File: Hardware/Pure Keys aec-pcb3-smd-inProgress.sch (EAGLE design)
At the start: 72 parts, among them Q2 20MHz, U1 ATMEGA328P_TQFP

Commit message: reroutes
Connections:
- net 5V: now also U1.VCC@6
- net GND: now also 75151-2A.D5, 75151-2A.D6, 75151-2A.D7, U1.AGND
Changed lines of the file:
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@@
 <part name="R2" library="rcl" deviceset="R-US_" device="R0805" value="330R"/>
 <part name="CLOCK" library="INSTRUO" deviceset="TRANSISTOR_MMBT3904" device="" value="2N3904"/>
-<part name="GND11" library="supply1" library_urn="urn:adsk.eagle:library:371" deviceset="GND" device=""/>
 <part name="R5" library="rcl" deviceset="R-US_" device="R0805" value="10K"/>
-<part name="SUPPLY9" library="supply2" deviceset="+5V" device=""/>
 <part name="R6" library="rcl" deviceset="R-US_" device="R0805" value="100K"/>
 <part name="R7" library="rcl" deviceset="R-US_" device="R0805" value="1M"/>
-<part name="GND12" library="supply1" library_urn="urn:adsk.eagle:library:371" deviceset="GND" device=""/>
 <part name="CLK_IN" library="GMSN" deviceset="PJ302M" device="" value="PJ302M"/>
-<part name="GND13" library="supply1" library_urn="urn:adsk.eagle:library:371" deviceset="GND" device=""/>
 <part name="REF" library="GMSN-R2Project" deviceset="LM4040A30IDBZT" device="" value="LM4040">
 <attribute name="MPN" value="LM4040A30IDBZT"/>
@@
 </segment>
 <segment>
-<wire x1="17.78" y1="111.76" x2="15.24" y2="111.76" width="0.1524" layer="91"/>
-<wire x1="15.24" y1="111.76" x2="15.24" y2="109.22" width="0.1524" layer="91"/>
-<wire x1="15.24" y1="109.22" x2="17.78" y2="109.22" width="0.1524" layer="91"/>
-<wire x1="15.24" y1="109.22" x2="12.7" y2="109.22" width="0.1524" layer="91"/>
-<junction x="15.24" y="109.22"/>
-<label x="12.7" y="109.22" size="1.778" layer="95" rot="R180"/>
-<pinref part="U1" gate="U$1" pin="GND@3"/>
-<pinref part="U1" gate="U$1" pin="GND@5"/>
-</segment>
-<segment>
 <pinref part="C17" gate="G$1" pin="2"/>
 <wire x1="-5.08" y1="142.24" x2="-10.16" y2="142.24" width="0.1524" layer="91"/>
@@
 <label x="165.1" y="83.82" size="1.778" layer="95"/>
 </segment>
+<segment>
+<pinref part="75151-2" gate="A" pin="D5"/>
+<wire x1="208.28" y1="96.52" x2="205.74" y2="96.52" width="0.1524" layer="91"/>
+<label x="198.12" y="96.52" size="1.778" layer="95"/>
+</segment>
+<segment>
+<pinref part="75151-2" gate="A" pin="D6"/>
+<wire x1="208.28" y1="93.98" x2="205.74" y2="93.98" width="0.1524" layer="91"/>
+<label x="198.12" y="93.98" size="1.778" layer="95"/>
+</segment>
+<segment>
+<pinref part="75151-2" gate="A" pin="D7"/>
+<wire x1="208.28" y1="91.44" x2="205.74" y2="91.44" width="0.1524" layer="91"/>
+<label x="198.12" y="91.44" size="1.778" layer="95"/>
+</segment>
+<segment>
+<pinref part="U1" gate="U$1" pin="GND@5"/>
+<wire x1="17.78" y1="109.22" x2="15.24" y2="109.22" width="0.1524" layer="91"/>
+<pinref part="U1" gate="U$1" pin="GND@3"/>
+<wire x1="15.24" y1="109.22" x2="10.16" y2="109.22" width="0.1524" layer="91"/>
+<wire x1="17.78" y1="111.76" x2="15.24" y2="111.76" width="0.1524" layer="91"/>
+<wire x1="15.24" y1="111.76" x2="15.24" y2="109.22" width="0.1524" layer="91"/>
+<junction x="15.24" y="109.22"/>
+<pinref part="U1" gate="U$1" pin="AGND"/>
+<wire x1="17.78" y1="114.3" x2="15.24" y2="114.3" width="0.1524" layer="91"/>
+<wire x1="15.24" y1="114.3" x2="15.24" y2="111.76" width="0.1524" layer="91"/>
+<junction x="15.24" y="111.76"/>
+<label x="10.16" y="109.22" size="1.778" layer="95"/>
+</segment>
 </net>
 <net name="RST" class="0">
@@
 <segment>
 <label x="15.24" y="165.1" size="1.778" layer="95" rot="R180"/>
-<wire x1="20.32" y1="165.1" x2="17.78" y2="165.1" width="0.1524" layer="91"/>
 <pinref part="U1" gate="U$1" pin="PC6(/RESET)"/>
 <wire x1="17.78" y1="165.1" x2="15.24" y2="165.1" width="0.1524" layer="91"/>
-<junction x="17.78" y="165.1"/>
 </segment>
 </net>
@@
 </segment>
 <segment>
-<wire x1="17.78" y1="160.02" x2="15.24" y2="160.02" width="0.1524" layer="91"/>
-<wire x1="17.78" y1="157.48" x2="15.24" y2="157.48" width="0.1524" layer="91"/>
-<wire x1="15.24" y1="157.48" x2="15.24" y2="160.02" width="0.1524" layer="91"/>
-<junction x="15.24" y="160.02"/>
-<label x="12.7" y="160.02" size="1.778" layer="95" rot="R180"/>
-<wire x1="15.24" y1="160.02" x2="12.7" y2="160.02" width="0.1524" layer="91"/>
-<pinref part="U1" gate="U$1" pin="VCC@4"/>
-<pinref part="U1" gate="U$1" pin="AVCC"/>
-</segment>
-<segment>
 <pinref part="74151-1" gate="P" pin="VCC"/>
 <wire x1="256.54" y1="162.56" x2="256.54" y2="165.1" width="0.1524" layer="91"/>
@@
 <wire x1="165.1" y1="101.6" x2="165.1" y2="104.14" width="0.1524" layer="91"/>
 <label x="165.1" y="104.14" size="1.778" layer="95"/>
+</segment>
+<segment>
+<pinref part="U1" gate="U$1" pin="AVCC"/>
+<wire x1="17.78" y1="160.02" x2="15.24" y2="160.02" width="0.1524" layer="91"/>
+<pinref part="U1" gate="U$1" pin="VCC@6"/>
+<wire x1="15.24" y1="160.02" x2="12.7" y2="160.02" width="0.1524" layer="91"/>
+<wire x1="17.78" y1="154.94" x2="15.24" y2="154.94" width="0.1524" layer="91"/>
+<wire x1="15.24" y1="154.94" x2="15.24" y2="157.48" width="0.1524" layer="91"/>
+<junction x="15.24" y="160.02"/>
+<pinref part="U1" gate="U$1" pin="VCC@4"/>
+<wire x1="15.24" y1="157.48" x2="15.24" y2="160.02" width="0.1524" layer="91"/>
+<wire x1="17.78" y1="157.48" x2="15.24" y2="157.48" width="0.1524" layer="91"/>
+<junction x="15.24" y="157.48"/>
+<label x="7.62" y="160.02" size="1.778" layer="95"/>
 </segment>
 </net>
@@
 <wire x1="99.06" y1="73.66" x2="81.28" y2="73.66" width="0.1524" layer="91"/>
 <junction x="99.06" y="73.66"/>
+<label x="73.66" y="73.66" size="1.778" layer="95"/>
 </segment>
 <segment>
@@
 <wire x1="99.06" y1="116.84" x2="81.28" y2="116.84" width="0.1524" layer="91"/>
 <junction x="99.06" y="116.84"/>
+<label x="76.2" y="116.84" size="1.778" layer="95"/>
 </segment>
 </net>
@@
 <instances>
 <instance part="CLOCK" gate="G$1" x="106.68" y="91.44" rot="R90"/>
-<instance part="GND11" gate="1" x="111.76" y="73.66" rot="MR0"/>
 <instance part="R5" gate="G$1" x="111.76" y="114.3" rot="MR90"/>
-<instance part="SUPPLY9" gate="+5V" x="111.76" y="124.46" rot="MR0"/>
 <instance part="R6" gate="G$1" x="78.74" y="91.44" rot="MR0"/>
 <instance part="R7" gate="G$1" x="88.9" y="83.82" rot="MR90"/>
-<instance part="GND12" gate="1" x="88.9" y="73.66" rot="MR0"/>
 <instance part="CLK_IN" gate="G$1" x="60.96" y="88.9" rot="MR0"/>
-<instance part="GND13" gate="1" x="68.58" y="81.28" rot="MR0"/>
 </instances>
 <busses>
 </busses>
 <nets>
-<net name="GND" class="1">
-<segment>
-<pinref part="CLOCK" gate="G$1" pin="E"/>
-<wire x1="111.76" y1="78.74" x2="111.76" y2="76.2" width="0.1524" layer="91"/>
-<pinref part="GND11" gate="1" pin="GND"/>
-</segment>
-<segment>
-<pinref part="R7" gate="G$1" pin="1"/>
-<wire x1="88.9" y1="78.74" x2="88.9" y2="76.2" width="0.1524" layer="91"/>
-<pinref part="GND12" gate="1" pin="GND"/>
-</segment>
-<segment>
-<pinref part="CLK_IN" gate="G$1" pin="SLEEVE"/>
-<wire x1="66.04" y1="86.36" x2="68.58" y2="86.36" width="0.1524" layer="91"/>
-<wire x1="68.58" y1="86.36" x2="68.58" y2="83.82" width="0.1524" layer="91"/>
-<pinref part="GND13" gate="1" pin="GND"/>
-</segment>
-</net>
 <net name="5V" class="1">
 <segment>
 <pinref part="R5" gate="G$1" pin="2"/>
-<pinref part="SUPPLY9" gate="+5V" pin="+5V"/>
 <wire x1="111.76" y1="121.92" x2="111.76" y2="119.38" width="0.1524" layer="91"/>
+<label x="111.76" y="121.92" size="1.778" layer="95"/>
 </segment>
 </net>
@@
 </segment>
 </net>
+<net name="GND" class="1">
+<segment>
+<pinref part="CLOCK" gate="G$1" pin="E"/>
+<wire x1="111.76" y1="78.74" x2="111.76" y2="76.2" width="0.1524" layer="91"/>
+<label x="111.76" y="76.2" size="1.778" layer="95"/>
+</segment>
+<segment>
+<pinref part="R7" gate="G$1" pin="1"/>
+<wire x1="88.9" y1="78.74" x2="88.9" y2="76.2" width="0.1524" layer="91"/>
+<label x="88.9" y="76.2" size="1.778" layer="95"/>
+</segment>
+<segment>
+<pinref part="CLK_IN" gate="G$1" pin="SLEEVE"/>
+<wire x1="66.04" y1="86.36" x2="68.58" y2="86.36" width="0.1524" layer="91"/>
+<wire x1="68.58" y1="86.36" x2="68.58" y2="83.82" width="0.1524" layer="91"/>
+<label x="68.58" y="83.82" size="1.778" layer="95"/>
+</segment>
+</net>

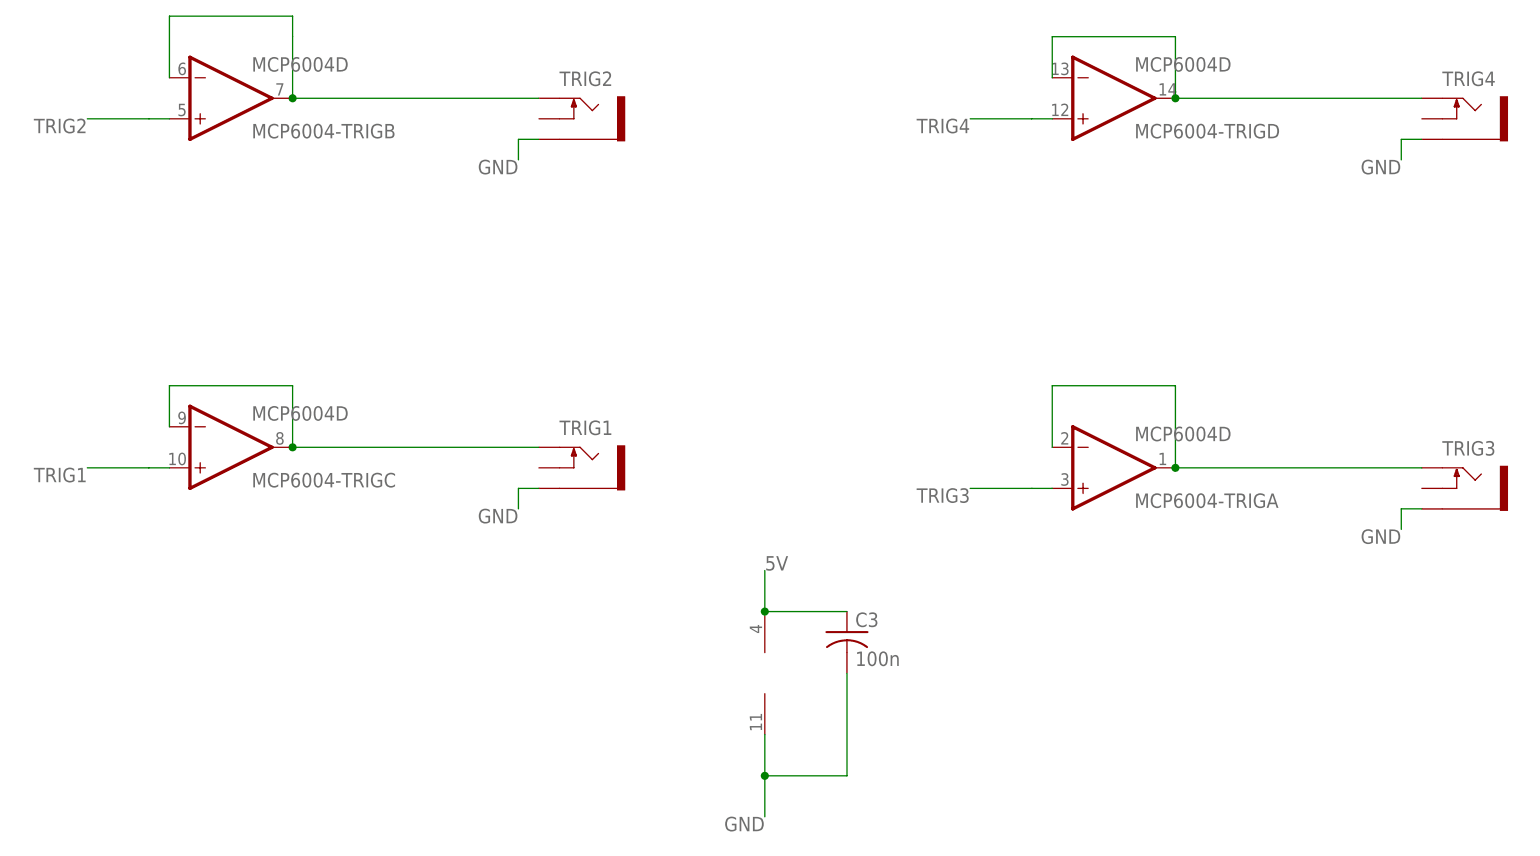
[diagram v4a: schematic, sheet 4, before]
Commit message: Replaced Sockets with vertical type
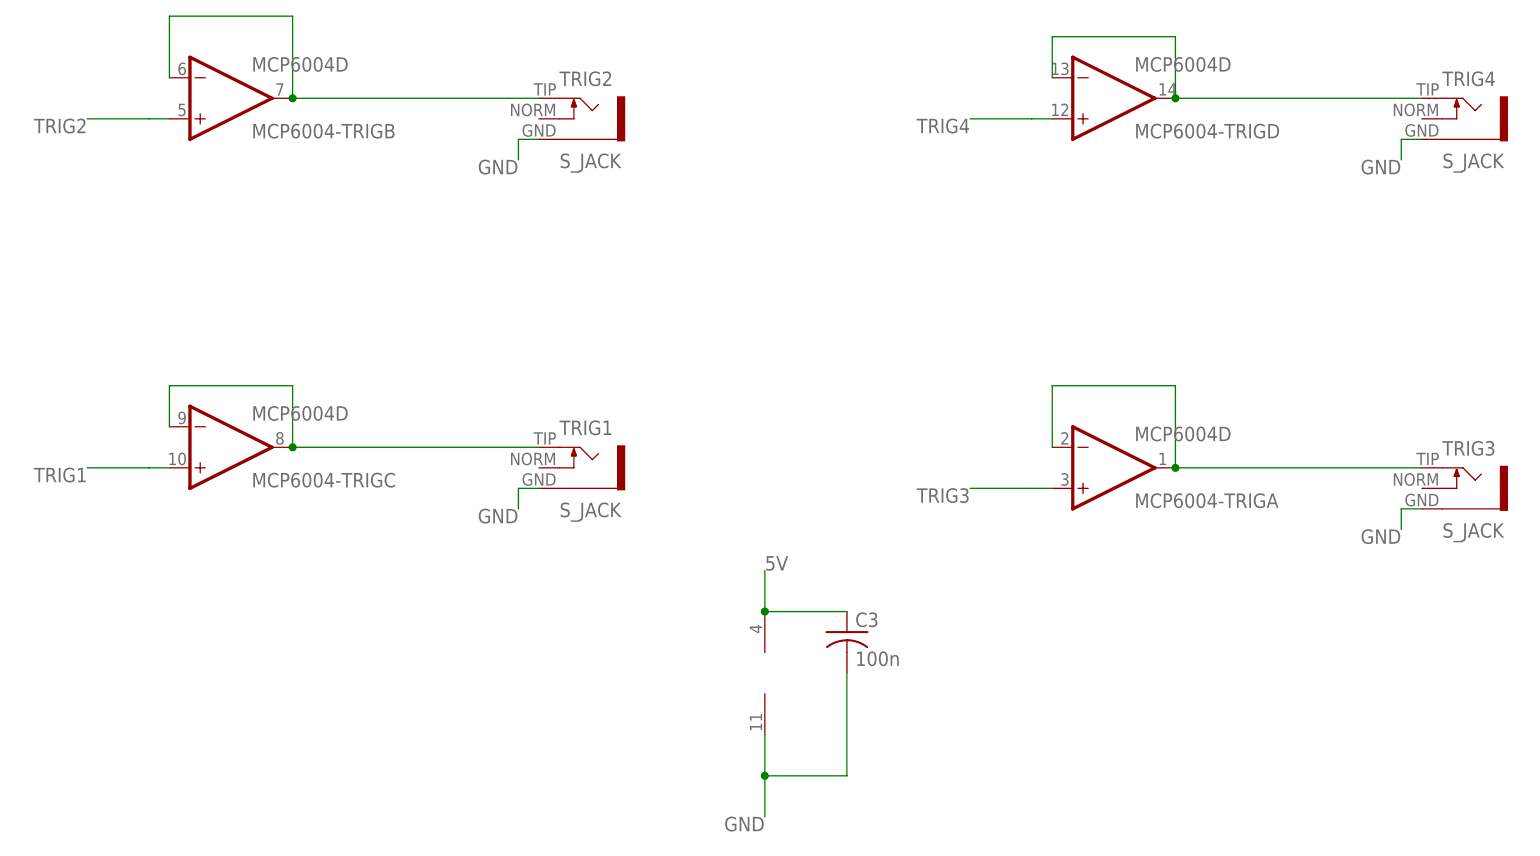
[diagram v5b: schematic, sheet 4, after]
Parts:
- CLK_IN, CV1, CV2, CV3, CV4, TRIG1, TRIG2, TRIG3, TRIG4: value PJ302M -> S_JACK; device GMSN:PJ302M -> INSTRUO:S_JACK
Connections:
- net GND: now also CLK_IN.GND, CV1.GND, CV2.GND, CV3.GND, CV4.GND, TRIG1.GND, TRIG2.GND, TRIG3.GND, TRIG4.GND; no longer CLK_IN.SLEEVE, CV1.SLEEVE, CV2.SLEEVE, CV3.SLEEVE, CV4.SLEEVE, TRIG1.SLEEVE, TRIG2.SLEEVE, TRIG3.SLEEVE, TRIG4.SLEEVE
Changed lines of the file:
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@@
 <class number="0" name="default" width="0" drill="0">
 </class>
-<class number="1" name="Power" width="0.8" drill="0">
+<class number="1" name="Power" width="0.6096" drill="0">
 </class>
 </classes>
@@
 <part name="ISP1" library="adafruit" deviceset="AVRISP" device="-6"/>
 <part name="C4" library="rcl" deviceset="CPOL-US" device="153CLV-0505" value="10u"/>
-<part name="CV1" library="GMSN" deviceset="PJ302M" device="" value="PJ302M"/>
-<part name="TRIG1" library="GMSN" deviceset="PJ302M" device="" value="PJ302M"/>
+<part name="CV1" library="INSTRUO" deviceset="S_JACK" device="" value="S_JACK"/>
+<part name="TRIG1" library="INSTRUO" deviceset="S_JACK" device="" value="S_JACK"/>
 <part name="R15" library="rcl" deviceset="R-US_" device="R0805" value="10K"/>
 <part name="R16" library="rcl" deviceset="R-US_" device="R0805" value="10K"/>
@@
 <attribute name="RS-PART" value="669-5364"/>
 </part>
-<part name="TRIG2" library="GMSN" deviceset="PJ302M" device="" value="PJ302M"/>
-<part name="TRIG3" library="GMSN" deviceset="PJ302M" device="" value="PJ302M"/>
-<part name="TRIG4" library="GMSN" deviceset="PJ302M" device="" value="PJ302M"/>
+<part name="TRIG2" library="INSTRUO" deviceset="S_JACK" device="" value="S_JACK"/>
+<part name="TRIG3" library="INSTRUO" deviceset="S_JACK" device="" value="S_JACK"/>
+<part name="TRIG4" library="INSTRUO" deviceset="S_JACK" device="" value="S_JACK"/>
 <part name="MCP6004-V" library="GMSN-R2Project" deviceset="MCP6004" device="D" value="MCP6004D"/>
-<part name="CV2" library="GMSN" deviceset="PJ302M" device="" value="PJ302M"/>
-<part name="CV3" library="GMSN" deviceset="PJ302M" device="" value="PJ302M"/>
-<part name="CV4" library="GMSN" deviceset="PJ302M" device="" value="PJ302M"/>
+<part name="CV2" library="INSTRUO" deviceset="S_JACK" device="" value="S_JACK"/>
+<part name="CV3" library="INSTRUO" deviceset="S_JACK" device="" value="S_JACK"/>
+<part name="CV4" library="INSTRUO" deviceset="S_JACK" device="" value="S_JACK"/>
 <part name="C6" library="rcl" deviceset="C-US" device="C0805K" value="10u"/>
 <part name="C11" library="rcl" deviceset="C-US" device="C0805K" value="100n"/>
@@
 <part name="R6" library="rcl" deviceset="R-US_" device="R0805" value="100K"/>
 <part name="R7" library="rcl" deviceset="R-US_" device="R0805" value="1M"/>
-<part name="CLK_IN" library="GMSN" deviceset="PJ302M" device="" value="PJ302M"/>
+<part name="CLK_IN" library="INSTRUO" deviceset="S_JACK" device="" value="S_JACK"/>
 <part name="REF" library="GMSN-R2Project" deviceset="LM4040A30IDBZT" device="" value="LM4040">
 <attribute name="MPN" value="LM4040A30IDBZT"/>
@@
 </busses>
 <nets>
-<net name="GND" class="0">
+<net name="GND" class="1">
 <segment>
 <pinref part="ISP1" gate="G$1" pin="GND"/>
@@
 </segment>
 </net>
-<net name="5V" class="0">
+<net name="5V" class="1">
 <segment>
 <pinref part="ISP1" gate="G$1" pin="VCC"/>
@@
 </busses>
 <nets>
-<net name="5V" class="0">
+<net name="5V" class="1">
 <segment>
 <pinref part="JP2" gate="G$1" pin="VBUS"/>
@@
 </segment>
 </net>
-<net name="GND" class="0">
+<net name="GND" class="1">
 <segment>
 <pinref part="JP2" gate="G$1" pin="GND"/>
@@
 </segment>
 </net>
-<net name="GND" class="0">
+<net name="GND" class="1">
 <segment>
 <pinref part="R18" gate="G$1" pin="1"/>
@@
 </busses>
 <nets>
-<net name="GND" class="0">
+<net name="GND" class="1">
 <segment>
 <pinref part="MCP6004-TRIG" gate="P" pin="V-"/>
@@
 </segment>
 <segment>
-<pinref part="TRIG2" gate="G$1" pin="SLEEVE"/>
+<pinref part="TRIG2" gate="G$1" pin="GND"/>
 <wire x1="91.44" y1="96.52" x2="88.9" y2="96.52" width="0.1524" layer="91"/>
 <wire x1="88.9" y1="96.52" x2="88.9" y2="93.98" width="0.1524" layer="91"/>
@@
 </segment>
 <segment>
-<pinref part="TRIG1" gate="G$1" pin="SLEEVE"/>
+<pinref part="TRIG1" gate="G$1" pin="GND"/>
 <wire x1="91.44" y1="53.34" x2="88.9" y2="53.34" width="0.1524" layer="91"/>
 <wire x1="88.9" y1="53.34" x2="88.9" y2="50.8" width="0.1524" layer="91"/>
@@
 </segment>
 <segment>
-<pinref part="TRIG4" gate="G$1" pin="SLEEVE"/>
+<pinref part="TRIG4" gate="G$1" pin="GND"/>
 <wire x1="200.66" y1="96.52" x2="198.12" y2="96.52" width="0.1524" layer="91"/>
 <wire x1="198.12" y1="96.52" x2="198.12" y2="93.98" width="0.1524" layer="91"/>
@@
 </segment>
 <segment>
-<pinref part="TRIG3" gate="G$1" pin="SLEEVE"/>
+<pinref part="TRIG3" gate="G$1" pin="GND"/>
 <wire x1="200.66" y1="50.8" x2="198.12" y2="50.8" width="0.1524" layer="91"/>
 <wire x1="198.12" y1="50.8" x2="198.12" y2="48.26" width="0.1524" layer="91"/>
@@
 </segment>
 </net>
-<net name="5V" class="0">
+<net name="5V" class="1">
 <segment>
 <pinref part="C3" gate="G$1" pin="1"/>
@@
 </segment>
 </net>
-<net name="5V" class="0">
+<net name="5V" class="1">
 <segment>
 <pinref part="C6" gate="G$1" pin="1"/>
@@
 </segment>
 </net>
-<net name="GND" class="0">
-<segment>
-<pinref part="CV4" gate="G$1" pin="SLEEVE"/>
+<net name="GND" class="1">
+<segment>
+<pinref part="CV4" gate="G$1" pin="GND"/>
 <wire x1="157.48" y1="2.54" x2="154.94" y2="2.54" width="0.1524" layer="91"/>
 <wire x1="154.94" y1="2.54" x2="154.94" y2="-7.62" width="0.1524" layer="91"/>
@@
 </segment>
 <segment>
-<pinref part="CV3" gate="G$1" pin="SLEEVE"/>
+<pinref part="CV3" gate="G$1" pin="GND"/>
 <wire x1="157.48" y1="53.34" x2="157.48" y2="40.64" width="0.1524" layer="91"/>
 <label x="157.48" y="40.64" size="1.778" layer="95" rot="R180"/>
 </segment>
 <segment>
-<pinref part="CV2" gate="G$1" pin="SLEEVE"/>
+<pinref part="CV2" gate="G$1" pin="GND"/>
 <wire x1="157.48" y1="99.06" x2="157.48" y2="86.36" width="0.1524" layer="91"/>
 <label x="157.48" y="86.36" size="1.778" layer="95" rot="R180"/>
 </segment>
 <segment>
-<pinref part="CV1" gate="G$1" pin="SLEEVE"/>
+<pinref part="CV1" gate="G$1" pin="GND"/>
 <wire x1="160.02" y1="137.16" x2="160.02" y2="124.46" width="0.1524" layer="91"/>
 <label x="160.02" y="124.46" size="1.778" layer="95" rot="R180"/>
@@
 </segment>
 </net>
-<net name="GND" class="0">
+<net name="GND" class="1">
 <segment>
 <pinref part="GLIDE1" gate="G$1" pin="3"/>
@@
 </segment>
 </net>
-<net name="5V" class="0">
+<net name="5V" class="1">
 <segment>
 <pinref part="GLIDE1" gate="G$1" pin="1"/>
@@
 </busses>
 <nets>
-<net name="5V" class="0">
+<net name="5V" class="1">
 <segment>
 <pinref part="R5" gate="G$1" pin="2"/>
@@
 </segment>
 </net>
-<net name="GND" class="0">
+<net name="GND" class="1">
 <segment>
 <pinref part="CLOCK" gate="G$1" pin="E"/>
@@
 </segment>
 <segment>
-<pinref part="CLK_IN" gate="G$1" pin="SLEEVE"/>
+<pinref part="CLK_IN" gate="G$1" pin="GND"/>
 <wire x1="66.04" y1="86.36" x2="68.58" y2="86.36" width="0.1524" layer="91"/>
 <wire x1="68.58" y1="86.36" x2="68.58" y2="83.82" width="0.1524" layer="91"/>
